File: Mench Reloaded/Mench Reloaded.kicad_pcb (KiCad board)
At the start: 2 copper layers, 100 x 100 mm, 60 parts, among them IC1 DS1813, J1 XBUS_265, J10 FTDI serial, J11 Power Sel, J12 Int Sel, J13 VIA1 Port A, J14 VIA1 Port B, J2 TGx, J3 RAM CSB select, J4 P4x, J5 P5x, J6 P6x, J7 68c256 Sel, J8 DC Power, J9 EEPROM R/W, SW1 SW_Push, U1 W65C265SxQ, U2 68c128 SRAM, U3 28C256, U4 LM1117 TO-252-3, U5 74HC00, U6 W65C22SxP, Y1 32.768 kHz, Y2 3.6864 mHz

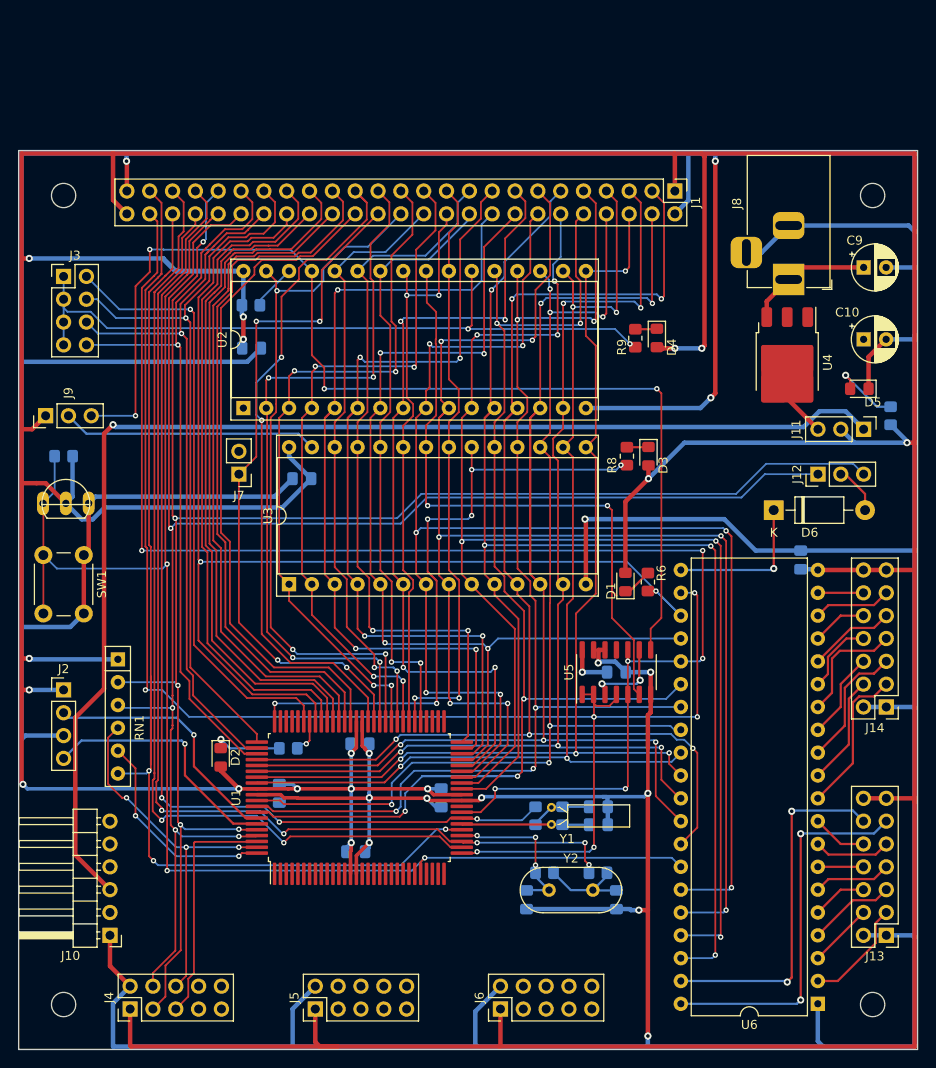
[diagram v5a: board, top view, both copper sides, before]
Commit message: Packed vertical traces more tightly. Aligned XBUS, J4, J5, J6, VIA 1, and VIA 2 with a 2.54mm grid
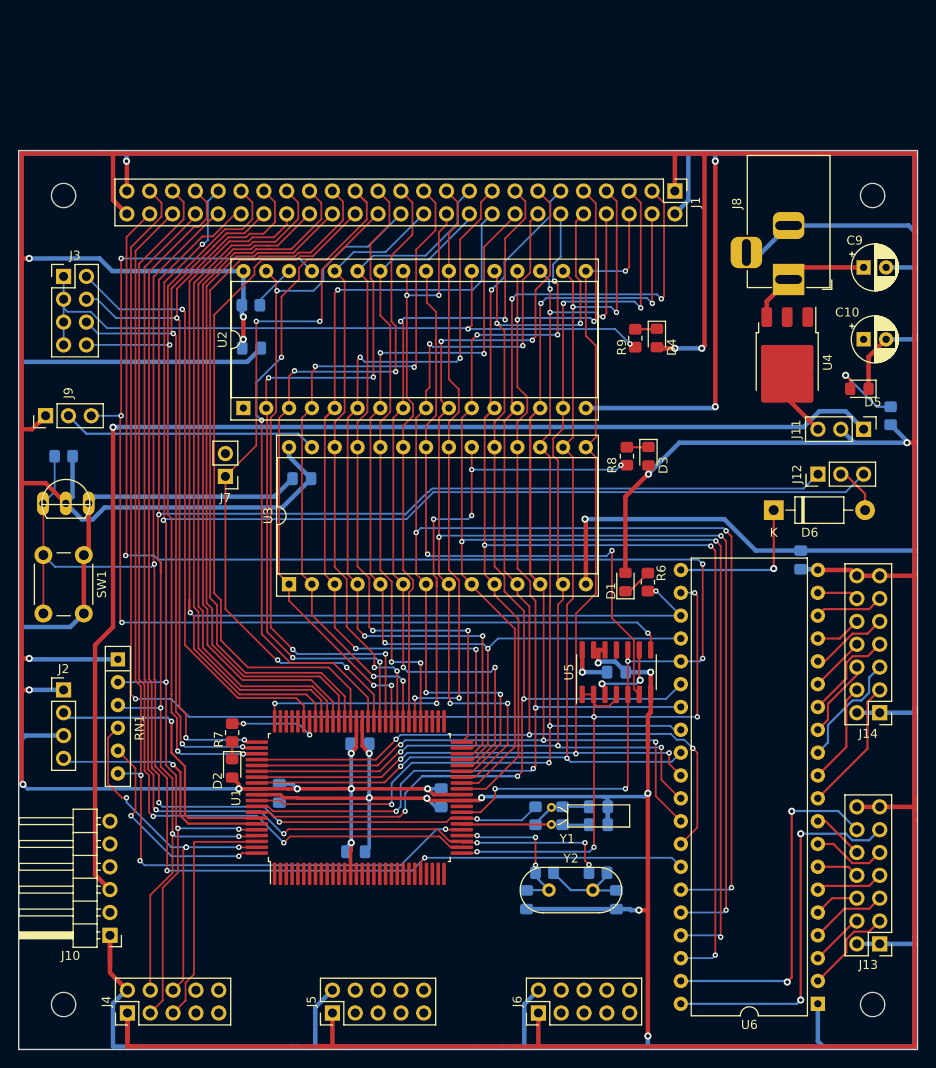
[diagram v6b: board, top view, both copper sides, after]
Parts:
- R7: moved to F.Cu
- moved R7 6.49 mm to (78.8, 109.8), turned to -90 degrees
- moved J6 4.24 mm to (112.8, 140.9)
- moved J5 1.96 mm to (89.9, 140.9)
- moved D2 1.77 mm to (78.8, 113.7)
- moved J7 1.52 mm to (78.0, 81.2)
- moved J13 1.20 mm to (150.8, 133.2)
- moved J14 0.97 mm to (150.8, 107.5)
- moved J4 0.53 mm to (67.1, 140.9)
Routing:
- net BE: track 123.0 -> 114.3 mm
- net csb2: track 3.86 -> 10.6 mm, vias 1 -> 2
- net +5V: track 666.4 -> 659.7 mm
- net Net-(D2-K): track 7.90 -> 1.95 mm, vias 1 -> 0
- net csb7: track 82.5 -> 87.4 mm, vias 1 -> 3
- net csb5: track 83.3 -> 87.3 mm, vias 1 -> 3
- net MEMOEB: track 75.7 -> 71.9 mm
- net csb6: track 79.8 -> 83.5 mm, vias 1 -> 3
- net MEMWEB: track 123.5 -> 126.7 mm
- net TG0: track 29.0 -> 32.2 mm
- net WEB: track 171.7 -> 174.1 mm
- net a19: track 75.3 -> 77.6 mm
- net Net-(J14-Pin_7): track 13.0 -> 10.8 mm
- net Net-(J10-Pin_3): track 140.2 -> 138.0 mm
- net Net-(J14-Pin_8): track 8.29 -> 6.24 mm
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
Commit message: Resized mounting holes to fit a 4-40 bolt. Aligned expansion headers so perf board will overlay them. Routed traces to J4, J5, and J6. Moved some resistors to the front of the board.
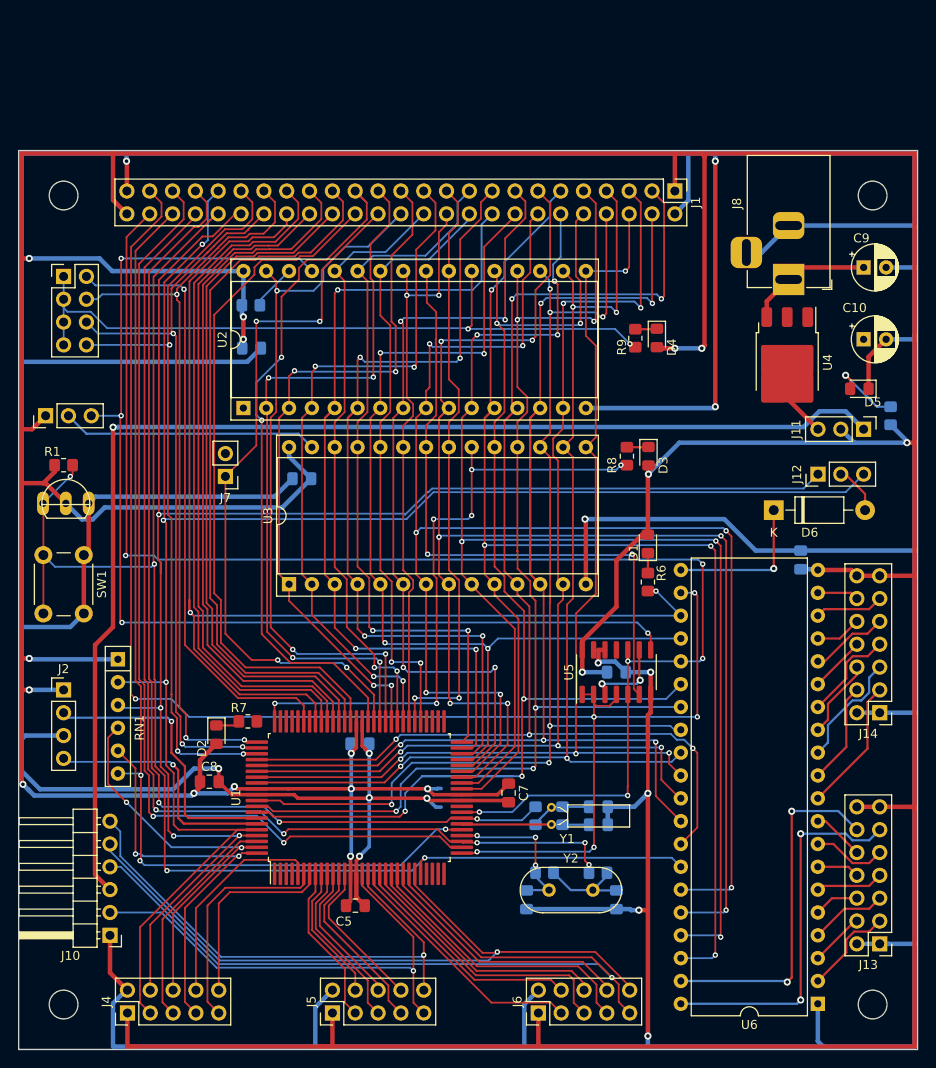
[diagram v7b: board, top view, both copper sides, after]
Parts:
- C5, C7, C8, R1: moved to F.Cu
- MH1, MH2, MH3, MH4: value MountingHole_2.7mm_M2.5_DIN965 -> MountingHole_3.2mm_M3_DIN965; footprint MountingHole:MountingHole_2.7mm_M2.5_DIN965 -> MountingHole:MountingHole_3.2mm_M3_DIN965
- moved C8 7.89 mm to (76.2, 115.2), turned to 0 degrees
- moved C7 7.52 mm to (109.5, 116.5)
- moved C5 6.00 mm to (92.5, 129.0)
- moved D1 4.93 mm to (125.0, 88.8)
- moved D2 4.14 mm to (77.0, 110.0)
- moved R7 2.15 mm to (80.5, 108.5), turned to 180 degrees
- moved R1 1.00 mm to (60.0, 80.0), turned to 180 degrees
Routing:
- net RXD3: track 0.00 -> 93.8 mm, vias 0 -> 1
- net TXD3: track 0.00 -> 79.6 mm, vias 0 -> 1
- net DSRB3: track 0.00 -> 58.4 mm, vias 0 -> 1
- net DTRB3: track 0.00 -> 54.8 mm, vias 0 -> 1
- net RXD2: track 0.00 -> 31.7 mm
- net RXD1: track 0.00 -> 30.7 mm
- net TXD2: track 0.00 -> 29.1 mm
- net TXD1: track 0.00 -> 28.0 mm
- net RXD0: track 0.00 -> 28.0 mm
- net TXD0: track 0.00 -> 26.3 mm
- net PIRS1: track 0.00 -> 25.3 mm
- net GND: track 740.7 -> 765.7 mm, vias 13 -> 14
- net PIRS0: track 0.00 -> 24.1 mm
- net AMS: track 24.3 -> 46.6 mm
- net PIRS2: track 0.00 -> 21.8 mm
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
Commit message: Changed EEPROM footprint to use low profile ZIF socket. Moved components and traces to make space for socket. Moved some resistors to the front side of the board.
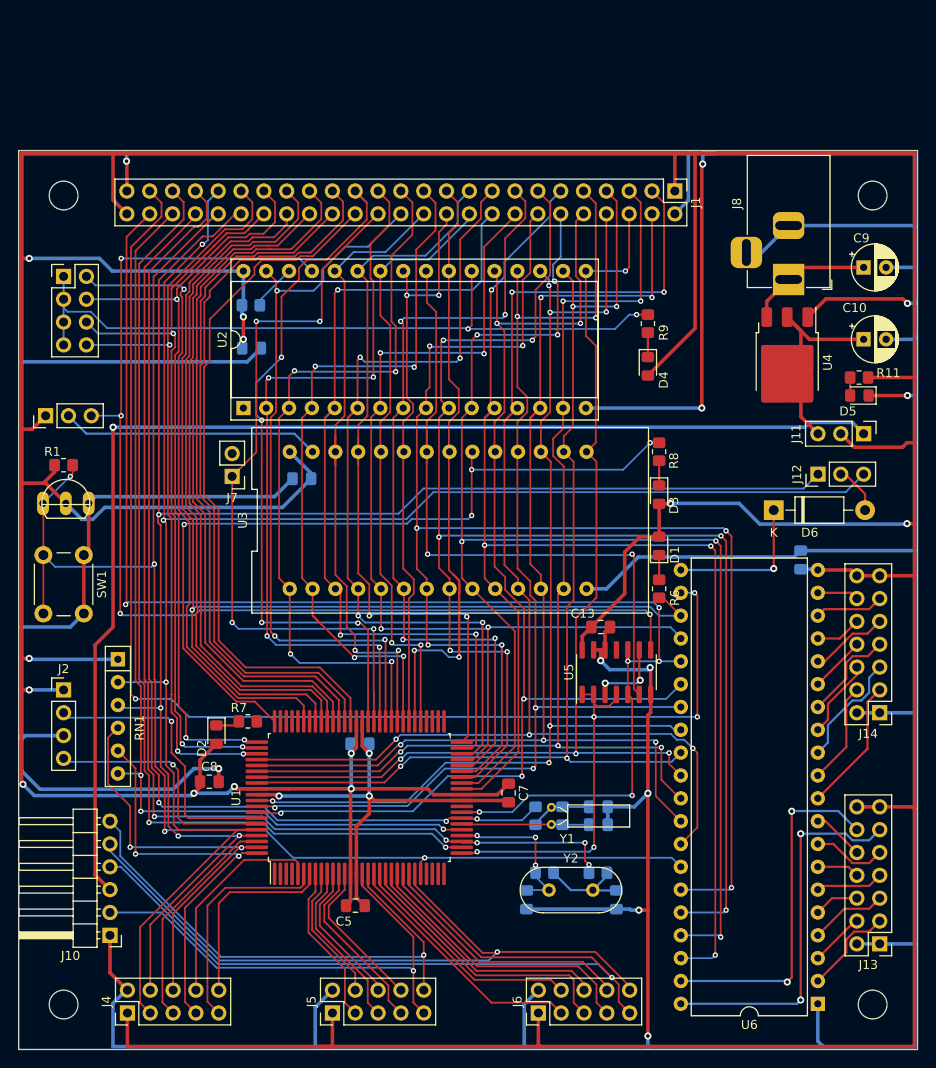
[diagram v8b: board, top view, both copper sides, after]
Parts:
- C13, R11: moved to F.Cu
- U3: footprint Package_DIP:DIP-28_W15.24mm_Socket -> Socket:DIP-28_W15.24mm_LowProfileZifSocket
- moved U3 18.0 mm to (101.7, 86.1), turned to 0 degrees
- moved R11 5.51 mm to (148.5, 70.2), turned to 180 degrees
- moved C13 5.32 mm to (119.8, 98.0)
- moved D3 4.44 mm to (126.2, 83.3)
- moved R8 3.62 mm to (126.2, 78.5), turned to -90 degrees
- moved D4 3.31 mm to (125.0, 69.0)
- moved R9 2.14 mm to (125.0, 64.2), turned to -90 degrees
- moved R6 1.46 mm to (126.2, 93.8)
- moved D1 1.27 mm to (126.2, 89.0)
- moved D5 0.75 mm to (148.5, 72.2)
- moved J7 0.75 mm to (78.8, 81.2)
- moved J11 0.50 mm to (149.0, 76.5)
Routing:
- net d7: track 152.1 -> 130.2 mm
- net csb4: track 70.1 -> 89.4 mm, vias 6 -> 4
- net d1: track 148.7 -> 130.4 mm
- net Net-(J11-Pin_3): track 7.59 -> 23.3 mm
- net a10: track 66.4 -> 77.1 mm
- net BE: track 114.3 -> 107.6 mm
- net Net-(D5-A): track 8.16 -> 2.00 mm, vias 1 -> 0
- net PHI2: track 158.1 -> 152.3 mm
- net a14: track 79.1 -> 84.2 mm
- net a13: track 67.7 -> 72.8 mm
- net +5V: track 675.7 -> 671.5 mm, vias 17 -> 12
- net a18: track 75.4 -> 79.1 mm, vias 2 -> 4
- net RESB: track 167.8 -> 164.3 mm
- net a8: track 82.4 -> 85.6 mm
- net a12: track 78.6 -> 81.6 mm
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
